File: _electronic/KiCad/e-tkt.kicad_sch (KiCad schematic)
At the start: 90 parts, among them J1 USB4105-GF-A, Q1 SS8050-G, Q2 SS8050-G, U1 USB6B1, U2 AZ1117I-3.3, U3 FT231XS, U4 ESP32-WROOM-32

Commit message: board silhouette and ftdi
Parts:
- removed C12, C9: 10uF, Capacitor_Tantalum_SMD:CP_EIA-3216-10_Kemet-I_Pad1.58x1.35mm_HandSolder, symbol Device:C_Polarized
- removed TP_IO15, TP_IO18, TP_IO5, TP_IO6, TP_IO7, TP_IO8: TestPoint, TestPoint:TestPoint_Pad_D1.0mm, symbol Connector:TestPoint
- added C12, C9: 10uF/25v, Capacitor_SMD:C_0603_1608Metric_Pad1.08x0.95mm_HandSolder, symbol Device:C
- added C13, C5: 47pF, Capacitor_SMD:C_0603_1608Metric_Pad1.08x0.95mm_HandSolder, symbol Device:C
- added C15, C16: 0.1uF, Capacitor_SMD:C_0603_1608Metric_Pad1.08x0.95mm_HandSolder, symbol Device:C
- added D_RX1, D_TX1: LED, LED_SMD:LED_0603_1608Metric_Pad1.05x0.95mm_HandSolder, symbol Device:LED
- added JP4, JP5, JP6, JP7: SolderJumper_2_Bridged, Jumper:SolderJumper-2_P1.3mm_Bridged2Bar_Pad1.0x1.5mm, symbol Jumper:SolderJumper_2_Bridged
- added R14, R19: 27R, Resistor_SMD:R_0603_1608Metric_Pad0.98x0.95mm_HandSolder, symbol Device:R
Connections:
- net +12V: now also J_USBPOWER1.2 (Pin_2), C12.2; no longer J_USBPOWER1.1 (Pin_1)
- net +3.3V: now also U3.13 (3V3OUT), U3.14 (~{RESET}), U3.3 (VCCIO), C16.1, C9.2, D_RX1.2 (A), D_TX1.2 (A)
- net +5V: now also J_USBPOWER1.1 (Pin_1), U3.15 (VCC), C15.1; no longer J_USBPOWER1.2 (Pin_2)
- net D+: now also C13.2, R19.2; no longer U3.11 (USBDP)
- net D-: now also C5.2, R14.2; no longer U3.12 (USBDM)
- net DTR: now also JP7.2 (B)
- net GNDREF: now also U3.16 (GND), C12.1, C13.1, C15.2, C16.2, C5.1, C9.1
- net RTS: now also JP6.2 (B)
- net at U3.1 (~{DTR}): now also JP7.1 (A)
- net at U3.10 (CBUS2): now also D_TX1.1 (K)
- net at U3.17 (CBUS1): now also D_RX1.1 (K)
- net at U3.2 (~{RTS}): now also JP6.1 (A)
- net IO12: no longer names the net of U4.14 (IO12)
- net IO13 renamed IO13 WIFI RST
- net IO14 renamed IO14 SERVO
- net IO15 renamed IO15 ULN 1
- net IO16 renamed IO16 ULN 4
- net IO17 renamed IO17 LED PRESS
- net IO18: no longer names the net of U4.30 (IO18)
- net IO19: no longer names the net of U4.31 (IO19)
- net IO2 renamed IO2 ULN 3
- net IO21 renamed IO21 OLED SDA
- net IO22 renamed IO22 OLED SCL
- net IO23: no longer names the net of U4.37 (IO23)
- net IO25 renamed IO25 NEMA ENA
- net IO26: no longer names the net of U4.11 (IO26)
- net IO27: no longer names the net of U4.12 (IO27)
- net IO32 renamed IO32 NEMA STEP
- net IO33 renamed IO33 NEMA DIR
- net IO34 renamed IO34 HALL
- net IO35: no longer names the net of U4.7 (IO35)
- net IO4 renamed IO4 ULN 2
- net IO5 renamed IO5 LED END
- net RXD0 IO3 renamed IO3 RXD
- net IO3 RXD: now also JP4.2 (B); no longer U3.20 (TXD)
- net TXD0 IO1 renamed IO1 TXD
- net IO1 TXD: now also JP5.2 (B); no longer U3.4 (RXD)
- new net: JP5.1 (A), U3.4 (RXD)
- new net: R14.1, U3.12 (USBDM)
- new net: R19.1, U3.11 (USBDP)
- new net: JP4.1 (A), U3.20 (TXD)
- no-connect marks 11 -> 32
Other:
- note added: "BOOT / RESET"
- note added: "FTDI"
- note added: "PADS"
- note removed: "RESET / BOOT"
- note removed: "TESTING"
- moved on the sheet: C10, C11, C2, C6, C7, D10, D11, D2, D5, D6, D7, D8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

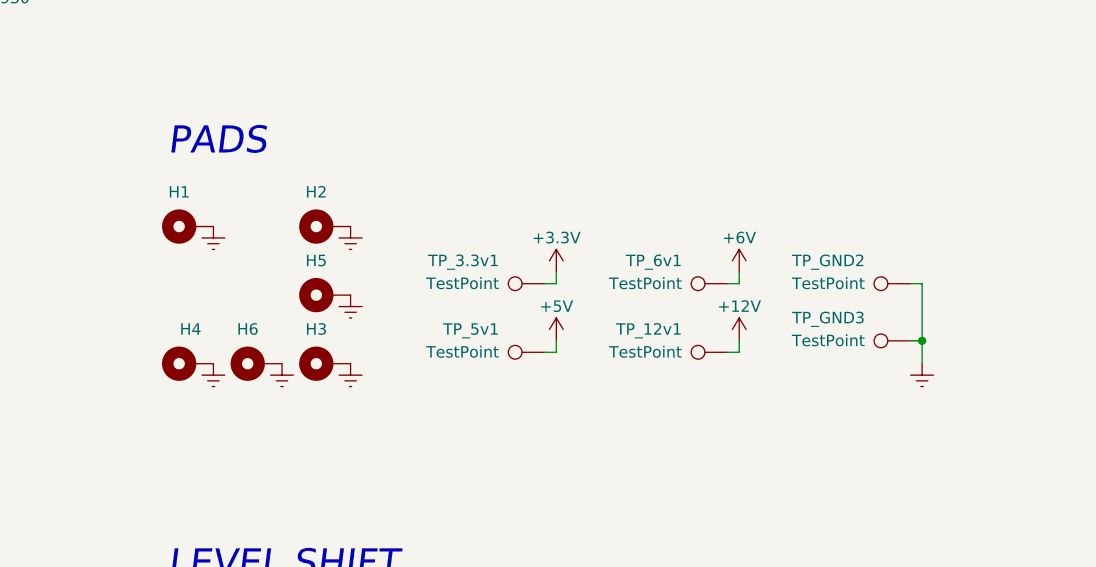
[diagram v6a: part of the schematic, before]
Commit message: board dimensions, taller
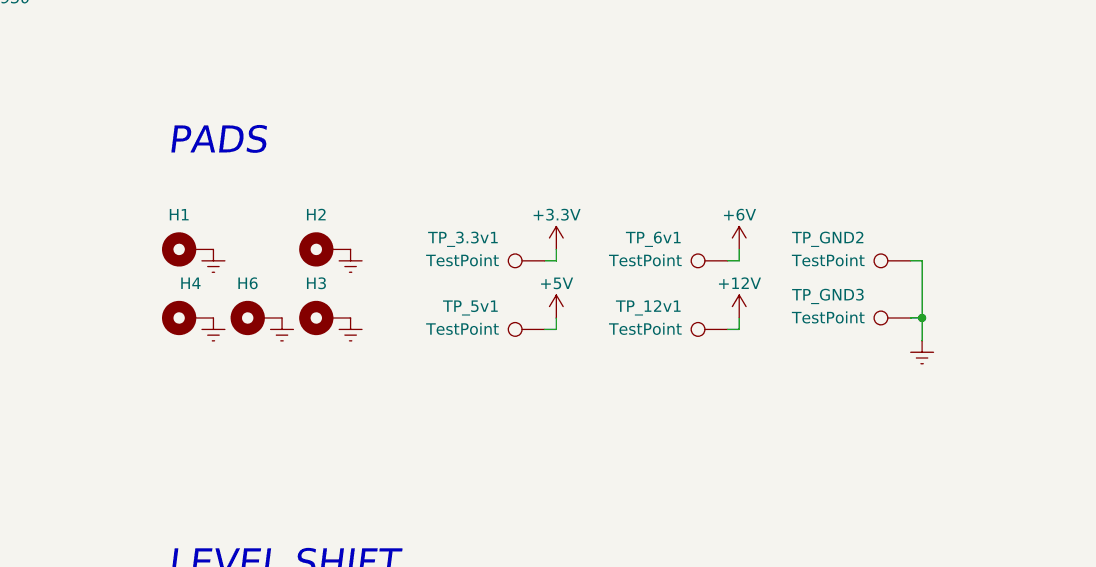
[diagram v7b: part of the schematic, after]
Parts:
- removed H5: MountingHole_Pad, MountingHole:MountingHole_3.2mm_M3_Pad_Via, symbol Mechanical:MountingHole_Pad
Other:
- moved on the sheet: H1, H2, H3, H4, H6, TP_12v1, TP_3.3v1, TP_5v1, TP_6v1, TP_GND2, TP_GND3

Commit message: improved decouple caps position, routing
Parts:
- removed JP1, JP2, JP3: SolderJumper_2_Bridged, Jumper:SolderJumper-2_P1.3mm_Bridged2Bar_Pad1.0x1.5mm, symbol Jumper:SolderJumper_2_Bridged
- added C14: 0.33uF, Capacitor_SMD:C_0603_1608Metric_Pad1.08x0.95mm_HandSolder, symbol Device:C
- added C17: 0.1uF, Capacitor_SMD:C_0603_1608Metric_Pad1.08x0.95mm_HandSolder, symbol Device:C
- added R20, R21: 0R, Resistor_SMD:R_0603_1608Metric, symbol Device:R
- C10: Id C1608X5R1E106M080AC -> (none)
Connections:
- net +12V: now also C14.1
- net +3.3V: now also A_DRIVER1.10 (MS1), A_DRIVER1.11 (MS2), A_DRIVER1.12 (MS3)
- net +6V: now also C17.1
- net GNDREF: now also D10.1 (K), D9.1 (K), C14.2, C17.2, R20.2, R21.2; no longer J_LED_END1.1 (Pin_1), J_LED_PRESS1.1 (Pin_1)
- net IO14 SERVO: now also Q_SERVO1.2 (S), R13.1
- net IO34 HALL: now also D9.2 (A), Q_HALL1.2 (S), R11.1; no longer D9.1 (K)
- new net: J_LED_END1.1 (Pin_1), R21.1
- new net: J_LED_PRESS1.1 (Pin_1), R20.1
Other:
- moved on the sheet: D10, D9, U_6v2
